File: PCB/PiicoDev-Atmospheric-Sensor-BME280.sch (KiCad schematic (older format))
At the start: 23 parts, among them J1 piico, J2 piico, J3 , U1 BME280

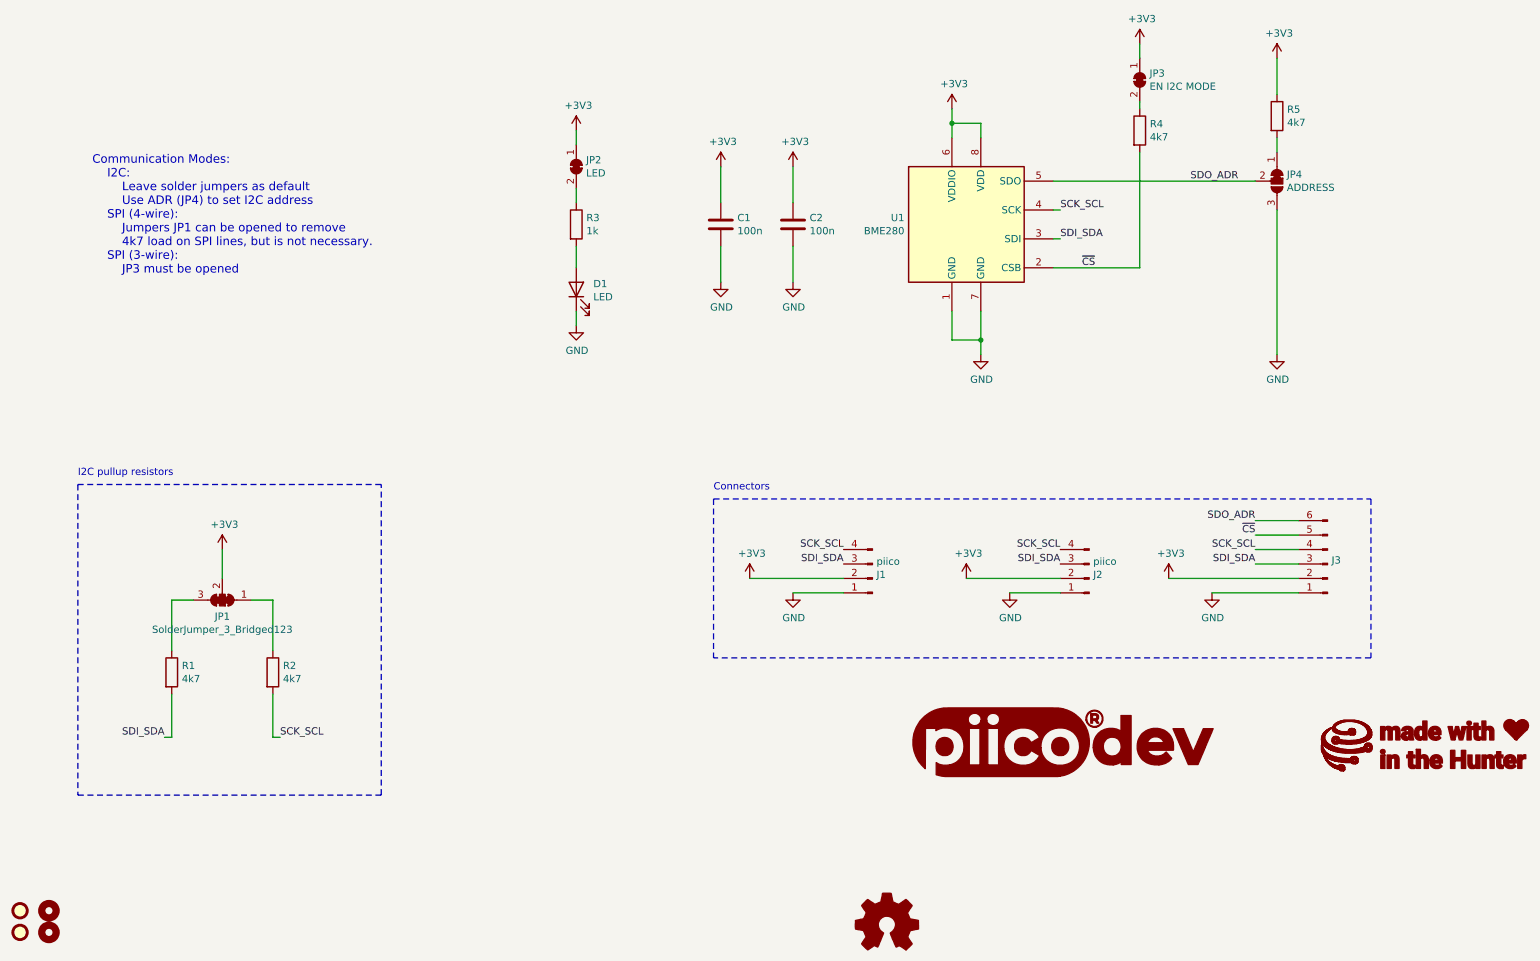
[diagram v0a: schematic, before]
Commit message: v11 Update
Change resistor values
Add DIP switch and remove ADR jumper
Update graphic labels
Remove solder mask between jumper pads
Update text formatting
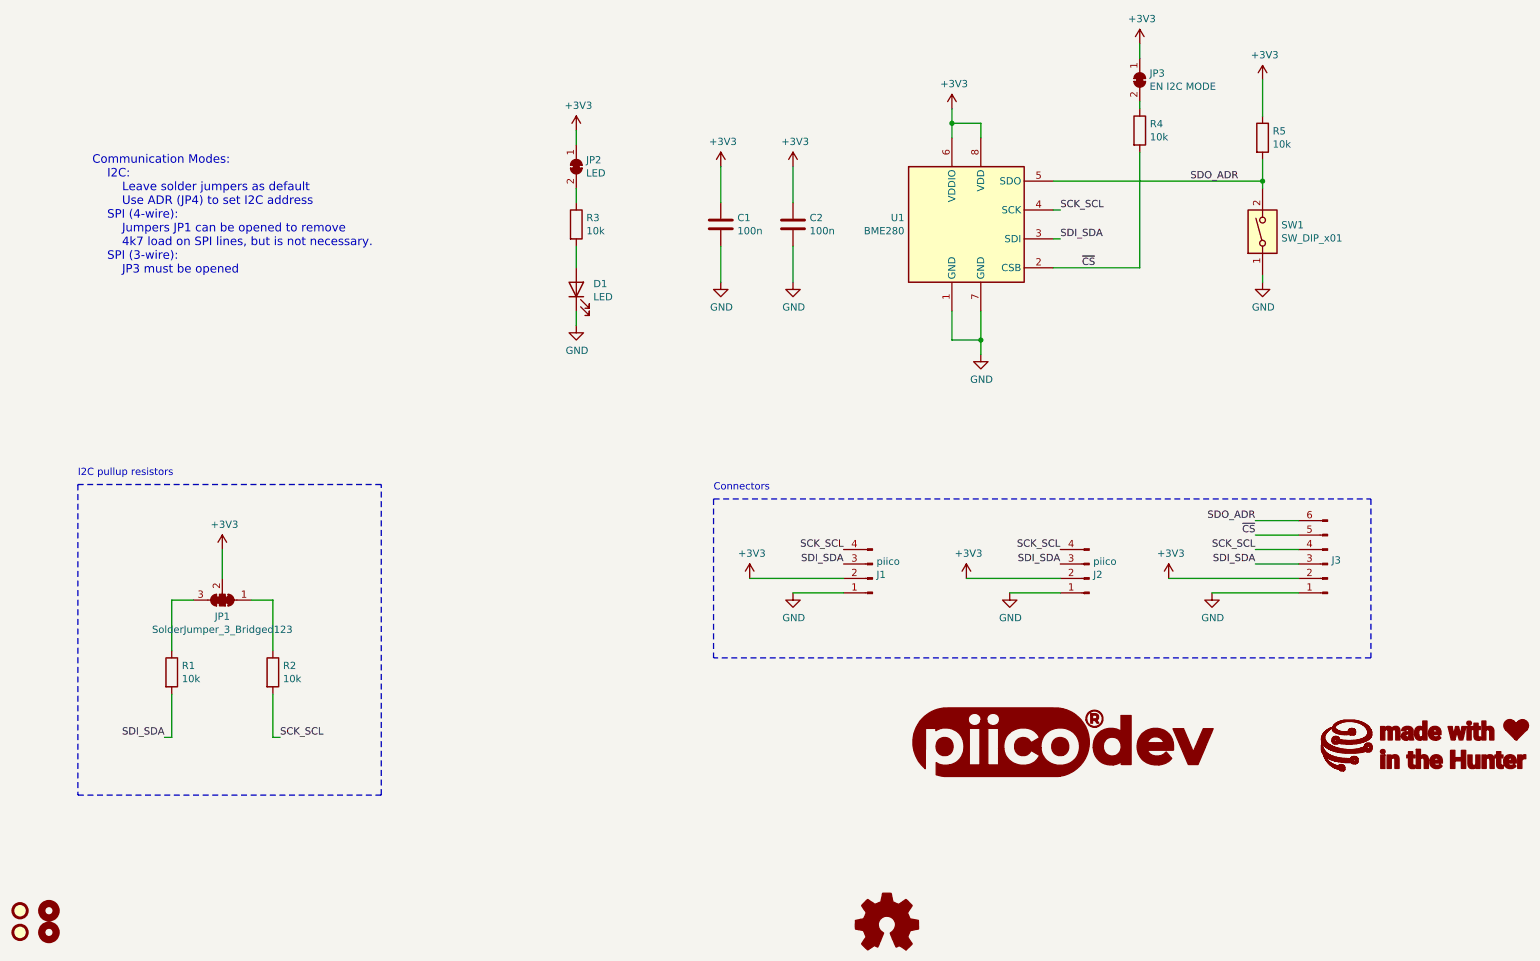
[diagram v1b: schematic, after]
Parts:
- removed G1: LOGO_CoreElectronics_made-with-love, CoreElectronics_Artwork:piicodev_logo_14.2x3.4mm, symbol CoreElectronics_Artwork:LOGO_CoreElectronics_made-with-love
- removed JP4: ADDRESS, Jumper:SolderJumper-3_P1.3mm_Bridged12_RoundedPad1.0x1.5mm, symbol Jumper:SolderJumper_3_Bridged12
- added G1: LOGO_CoreElectronics_no-text, CoreElectronics_Artwork:CoreElectronics_logo_5mm, symbol CoreElectronics_Artwork:LOGO_CoreElectronics_no-text
- added G3: LOGO_made-with-love, CoreElectronics_Artwork:piicodev_logo_14.2x3.4mm, symbol CoreElectronics_Artwork:LOGO_made-with-love
- added SW1: SW_DIP_x01, CoreElectronics_Components:SW_DIP_x01_Slide_CHS-01A1, symbol Switch:SW_DIP_x01
- JP1: footprint CoreElectronics_Connectors:SolderJumper-3_P1.3mm_Closed_RoundedPad1.0x1.5mm -> CoreElectronics_Components:SolderJumper-3_P1.3mm_Closed_RoundedPad1.0x1.5mm_NumberLabels
- JP2, JP3: footprint Jumper:SolderJumper-2_P1.3mm_Bridged_RoundedPad1.0x1.5mm -> CoreElectronics_Components:SolderJumper-2_P1.3mm_Bridged_RoundedPad1.0x1.5mm
- LOGO1: footprint CoreElectronics_Logos:oshw -> CoreElectronics_Artwork:oshw
- R1, R2, R4, R5: value 4k7 -> 10k
- R3: value 1k -> 10k
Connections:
- net GND: now also SW1.1
- net SDO_ADR: now also R5.2, SW1.2
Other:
- moved on the sheet: R5
